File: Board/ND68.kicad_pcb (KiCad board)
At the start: 2 copper layers, 3.4 x 3 mm, 38 parts, among them J1 USB_C_Receptacle_USB2.0_14P, J2 Conn_01x03_Pin, U1 NCP1117-3.3_SOT223, U2 RP2040, Y1 Crystal_GND24

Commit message: VERY BASIC pcb layout
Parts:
- D1, D2, D3, D4: moved to B.Cu
- moved SW1 88.9 mm to (169.6, 81.3)
- moved SW3 88.9 mm to (169.6, 100.3)
- moved SW2 88.9 mm to (188.6, 81.3)
- moved SW4 88.9 mm to (188.6, 100.3)
- moved J2 77.4 mm to (142.9, 109.6), turned to 180 degrees
- moved J1 76.5 mm to (148.1, 73.6), turned to 180 degrees
- moved C2 76.3 mm to (133.3, 87.4), turned to -90 degrees
- moved C1 74.8 mm to (137.2, 87.4), turned to -90 degrees
- moved C7 72.8 mm to (153.2, 92.7), turned to 90 degrees
- moved C6 70.7 mm to (151.6, 92.7), turned to 90 degrees
- moved R2 70.0 mm to (146.1, 81.1), turned to -90 degrees
- moved C3 69.5 mm to (150.7, 92.7), turned to 90 degrees
- moved R1 68.7 mm to (150.0, 81.1), turned to -90 degrees
- moved R5 67.8 mm to (149.4, 92.7), turned to -90 degrees
- moved R6 66.3 mm to (148.4, 92.7), turned to -90 degrees
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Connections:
- R1 pad 1: Net-(J1-CC2) -> Net-(J1-CC1)
- R2 pad 1: Net-(J1-CC1) -> Net-(J1-CC2)

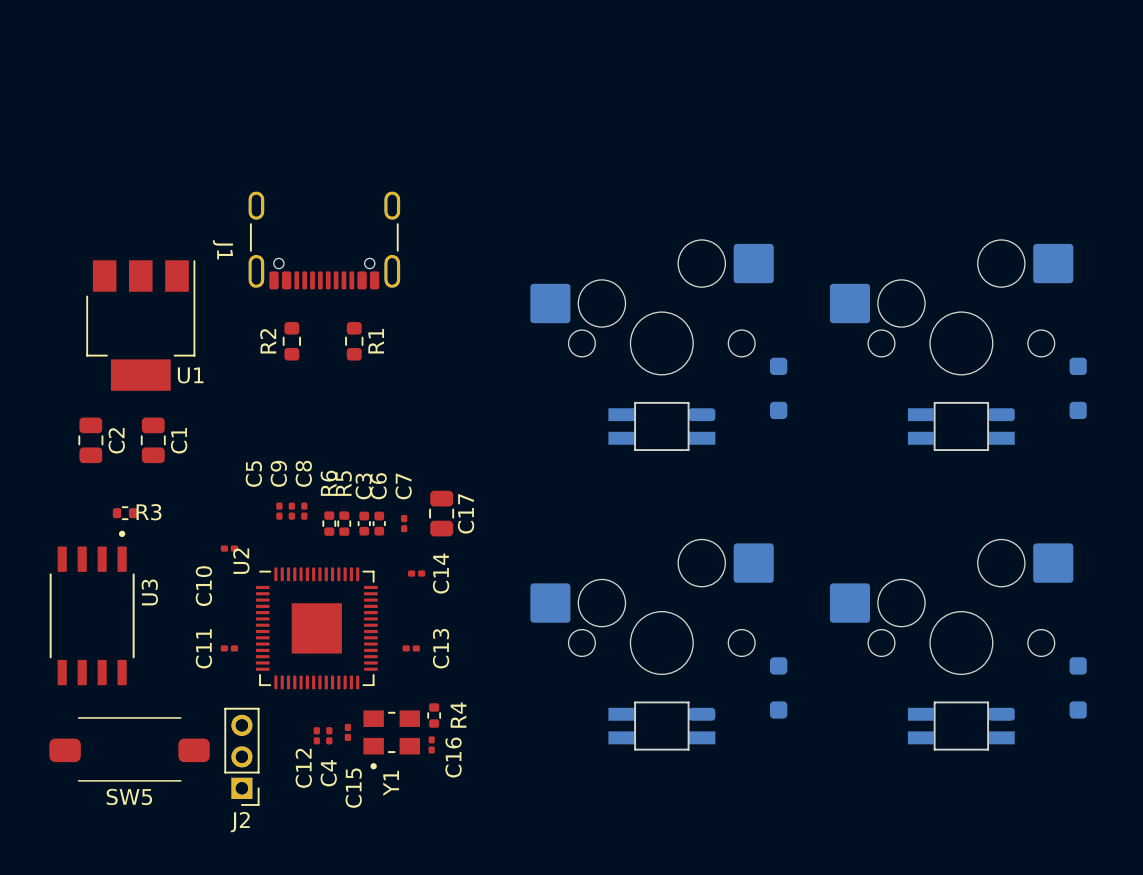
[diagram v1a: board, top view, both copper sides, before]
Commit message: Fixed pad numbers on 1u argb hotswap footprint and added a border to the pcb :)
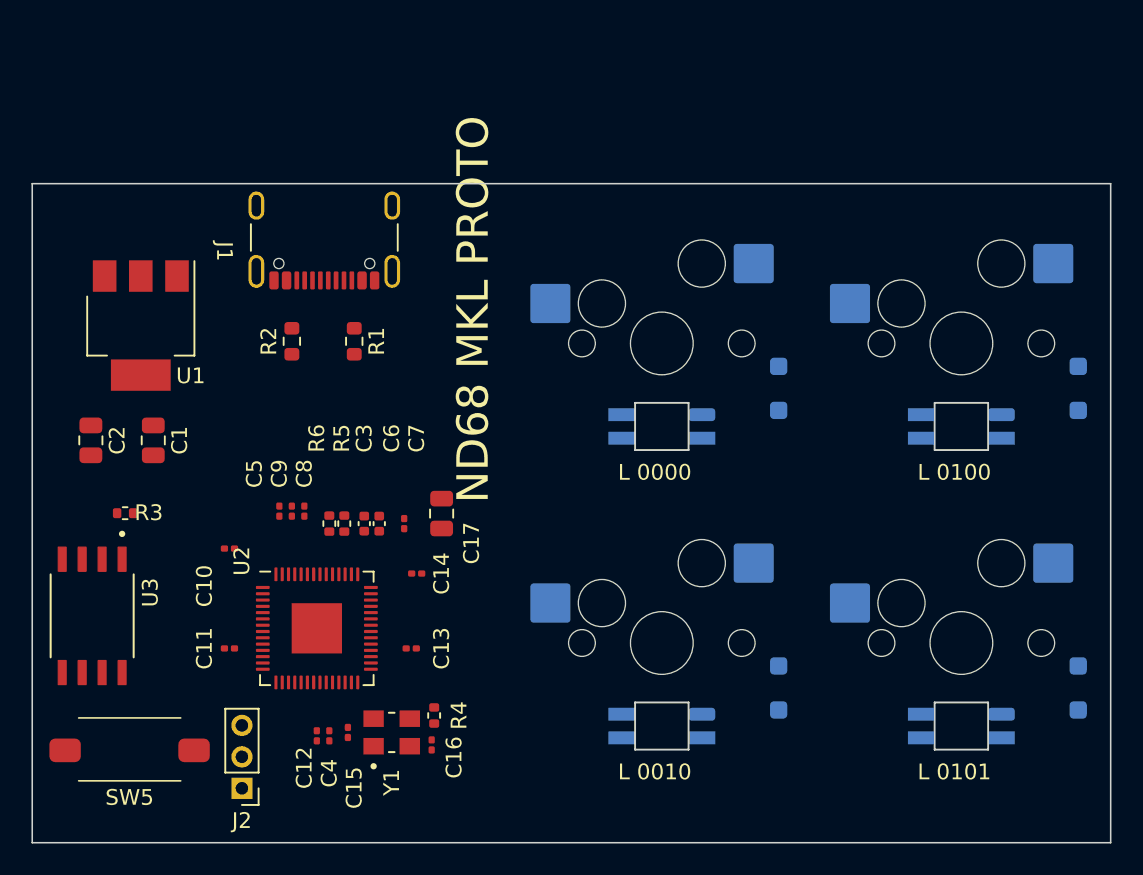
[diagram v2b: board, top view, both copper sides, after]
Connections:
- SW1 pad 1: (no net) -> VDD
- SW1 pad 2: (no net) -> Net-(SW1-DOUT)
- SW1 pad 3: (no net) -> GND
- SW1 pad 4: (no net) -> DIN
- SW2 pad 1: (no net) -> VDD
- SW2 pad 2: (no net) -> Net-(SW2-DOUT)
- SW2 pad 3: (no net) -> GND
- SW2 pad 4: (no net) -> Net-(SW1-DOUT)
- SW3 pad 1: (no net) -> VDD
- SW3 pad 2: (no net) -> Net-(SW3-DOUT)
- SW3 pad 3: (no net) -> GND
- SW3 pad 4: (no net) -> Net-(SW2-DOUT)
- SW4 pad 1: (no net) -> VDD
- SW4 pad 2: (no net) -> unconnected-(SW4-DOUT-Pad2)
- SW4 pad 3: (no net) -> GND
- SW4 pad 4: (no net) -> Net-(SW3-DOUT)
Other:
- board size 3.4 x 3 mm -> 68.6 x 41.9 mm
- board text added: "ND68 MKL PROTO"

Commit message: Route mcu
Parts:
- moved C17 19.7 mm to (141.2, 105.6), turned to -90 degrees
- moved C1 13.8 mm to (131.3, 75.0)
- moved J2 13.6 mm to (156.4, 108.0)
- moved R3 11.9 mm to (132.6, 103.6), turned to 90 degrees
- moved U3 9.19 mm to (138.9, 91.3), turned to 0 degrees
- moved C15 6.61 mm to (143.1, 107.2)
- moved C16 6.61 mm to (148.4, 108.0)
- moved R4 6.61 mm to (148.6, 106.1)
- moved Y1 6.61 mm to (145.9, 107.2)
- moved C2 4.12 mm to (135.2, 83.8)
- moved SW5 3.26 mm to (135.8, 103.9), turned to -90 degrees
- moved U1 3.15 mm to (136.5, 77.0)
- moved C12 2.93 mm to (150.5, 105.6), turned to 0 degrees
- moved C4 2.52 mm to (150.5, 104.8), turned to 0 degrees
- moved C10 2.38 mm to (142.0, 96.7)
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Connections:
- SW1 pad 5: (no net) -> Net-(D1-A)
- SW1 pad 6: (no net) -> C0
- SW2 pad 5: (no net) -> Net-(D2-A)
- SW2 pad 6: (no net) -> C1
- SW3 pad 5: (no net) -> Net-(D4-A)
- SW3 pad 6: (no net) -> C0
- SW4 pad 5: (no net) -> Net-(D3-A)
- SW4 pad 6: (no net) -> C1
- SW5 pad 1: (no net) -> GND
- SW5 pad 2: (no net) -> Net-(R3-Pad1)
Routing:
- net +3.3V: track 0.00 -> 33.3 mm
- net QSPI_SS: track 0.00 -> 27.5 mm
- net QSPI_SD1: track 0.00 -> 17.0 mm
- net D+: track 0.00 -> 14.7 mm
- net D-: track 0.00 -> 14.6 mm
- net QSPI_SD2: track 0.00 -> 12.8 mm
- net Net-(J2-Pin_1): track 0.00 -> 11.2 mm
- net +1V1: track 0.00 -> 10.6 mm
- net Net-(J2-Pin_3): track 0.00 -> 8.11 mm
- net XIN: track 0.00 -> 8.01 mm
- net QSPI_SD3: track 0.00 -> 7.57 mm
- net QSPI_SCLK: track 0.00 -> 6.55 mm
- net QSPI_SD0: track 0.00 -> 5.53 mm
- net Net-(R3-Pad1): track 0.00 -> 5.19 mm
- net GND: track 0.00 -> 3.60 mm
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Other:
- board size 68.6 x 41.9 mm -> 69.4 x 40.3 mm
- board text added: "CLK SWD"

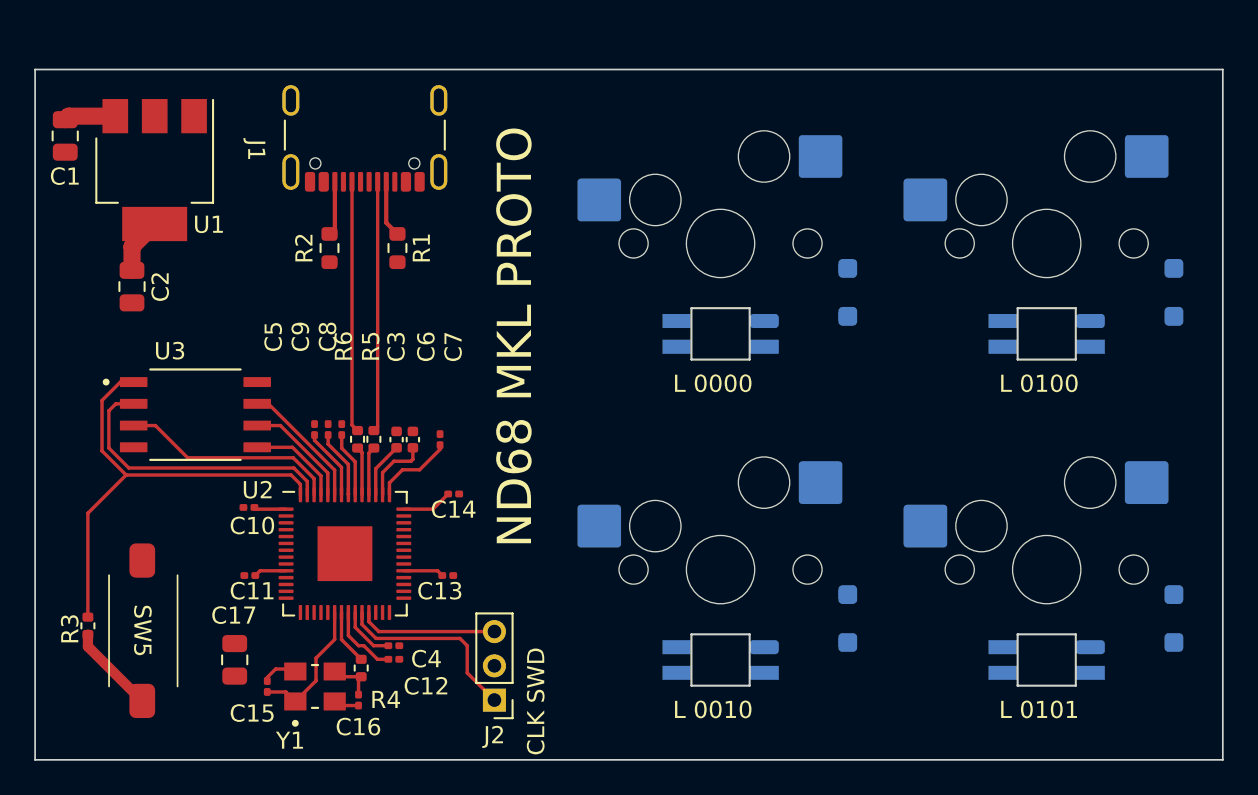
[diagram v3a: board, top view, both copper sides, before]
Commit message: Done routing all parts.
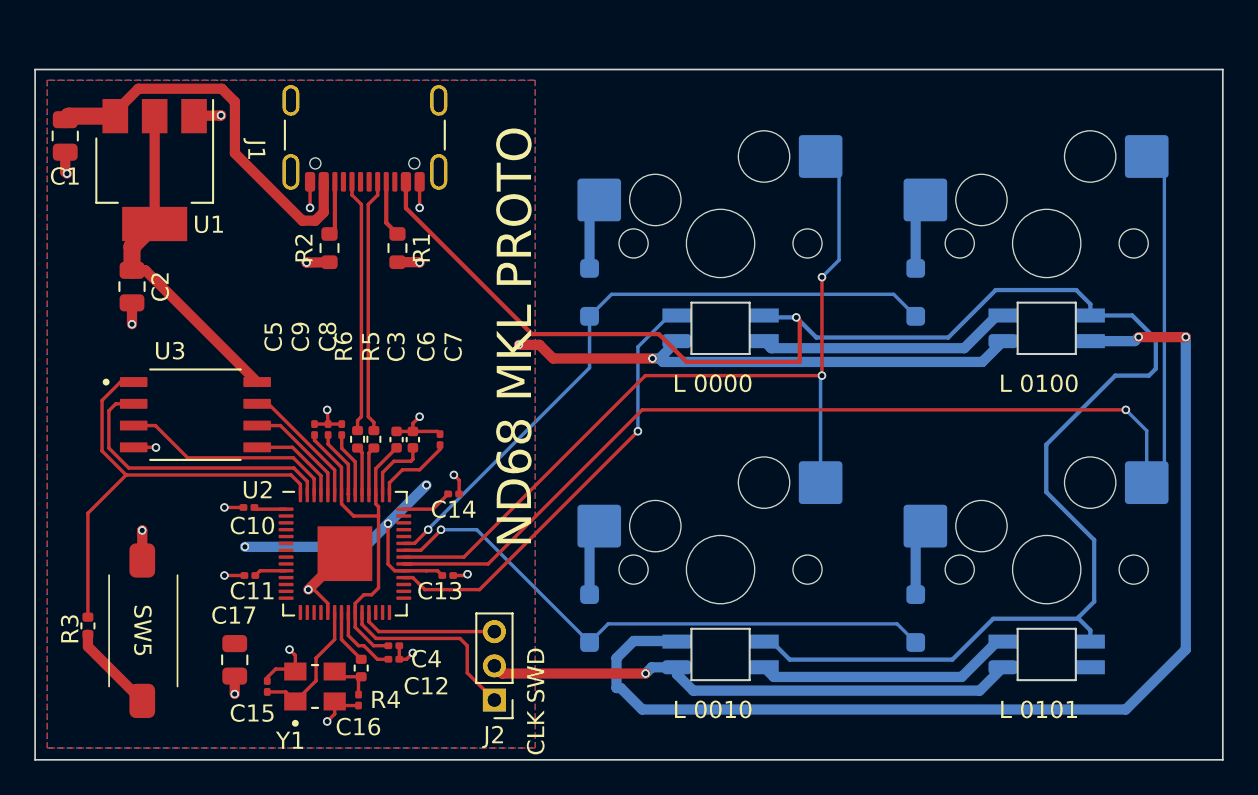
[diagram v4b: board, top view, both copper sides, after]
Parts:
- added G***: LOGO, ND68:troll, B.Cu at (143.8, 87.8)
- moved D2 15.1 mm to (181.0, 84.1)
- moved D4 15.1 mm to (181.0, 103.2)
- moved D1 15.1 mm to (161.9, 84.1)
- moved D3 15.1 mm to (161.9, 103.2)
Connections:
- SW1 pad 1: VDD -> VBUS
- SW2 pad 1: VDD -> VBUS
- SW3 pad 1: VDD -> VBUS
- SW3 pad 5: Net-(D4-A) -> Net-(D3-A)
- SW4 pad 1: VDD -> VBUS
- SW4 pad 5: Net-(D3-A) -> Net-(D4-A)
- U2 pad 32: unconnected-(U2-GPIO21-Pad32) -> DIN
- U2 pad 34: unconnected-(U2-GPIO22-Pad34) -> C1
- U2 pad 35: unconnected-(U2-GPIO23-Pad35) -> C0
- U2 pad 36: unconnected-(U2-GPIO24-Pad36) -> R1
- U2 pad 37: unconnected-(U2-GPIO25-Pad37) -> R0
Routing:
- net VBUS: track 3.01 -> 123.5 mm, vias 0 -> 1
- net GND: track 3.60 -> 99.3 mm, vias 0 -> 23
- net C1: track 0.00 -> 71.0 mm, vias 0 -> 1
- net Net-(SW2-DOUT): track 0.00 -> 64.8 mm, vias 0 -> 2
- net C0: track 0.00 -> 50.3 mm, vias 0 -> 2
- net R0: track 0.00 -> 38.2 mm, vias 0 -> 1
- net R1: track 0.00 -> 34.0 mm, vias 0 -> 1
- net +3.3V: track 33.3 -> 65.3 mm, vias 0 -> 3
- net DIN: track 0.00 -> 25.8 mm, vias 0 -> 1
- net Net-(SW3-DOUT): track 0.00 -> 15.0 mm
- net Net-(SW1-DOUT): track 0.00 -> 14.9 mm
- net +1V1: track 10.6 -> 21.4 mm
- net Net-(D2-A): track 0.00 -> 4.23 mm
- net Net-(D4-A): track 0.00 -> 4.23 mm
- net Net-(D1-A): track 0.00 -> 4.23 mm
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- added copper zone on F.Cu, net +3.3V
- added copper zone on B.Cu, net GND

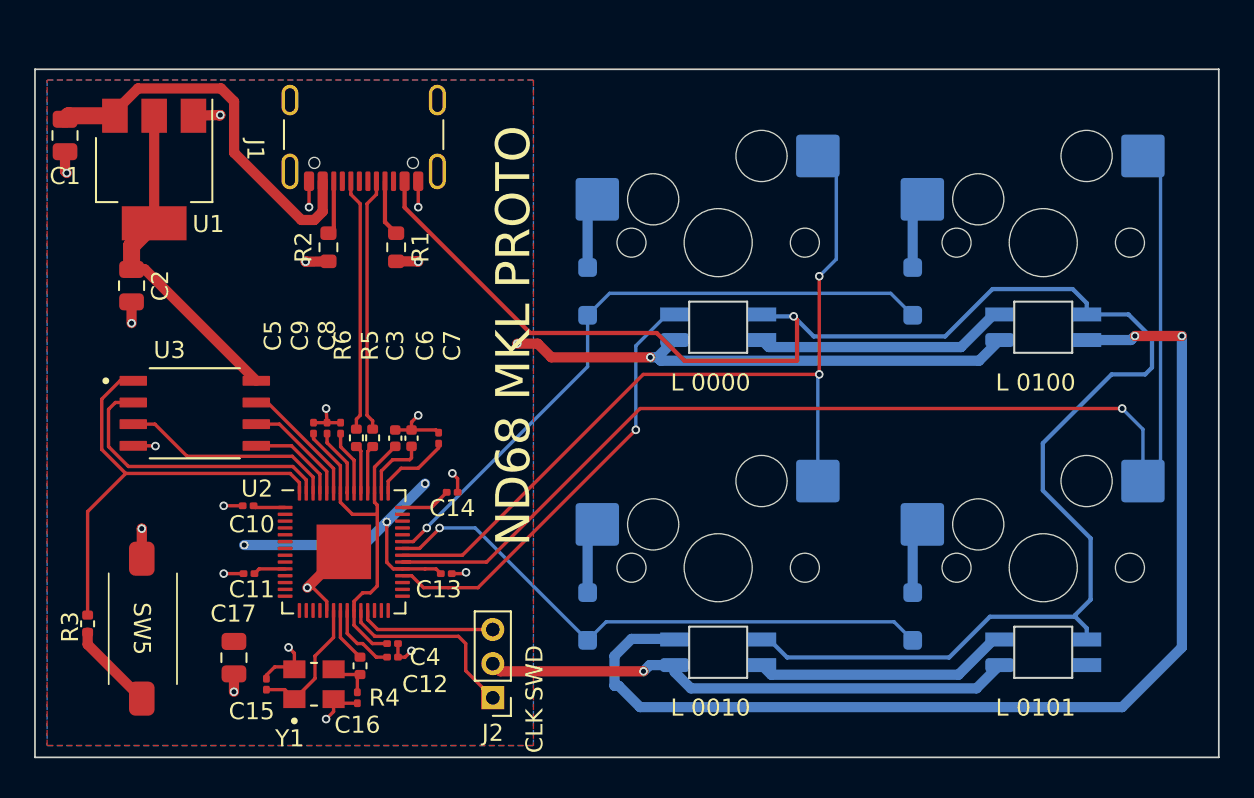
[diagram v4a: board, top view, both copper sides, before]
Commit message: Fixed coupling issues and cleaned up board
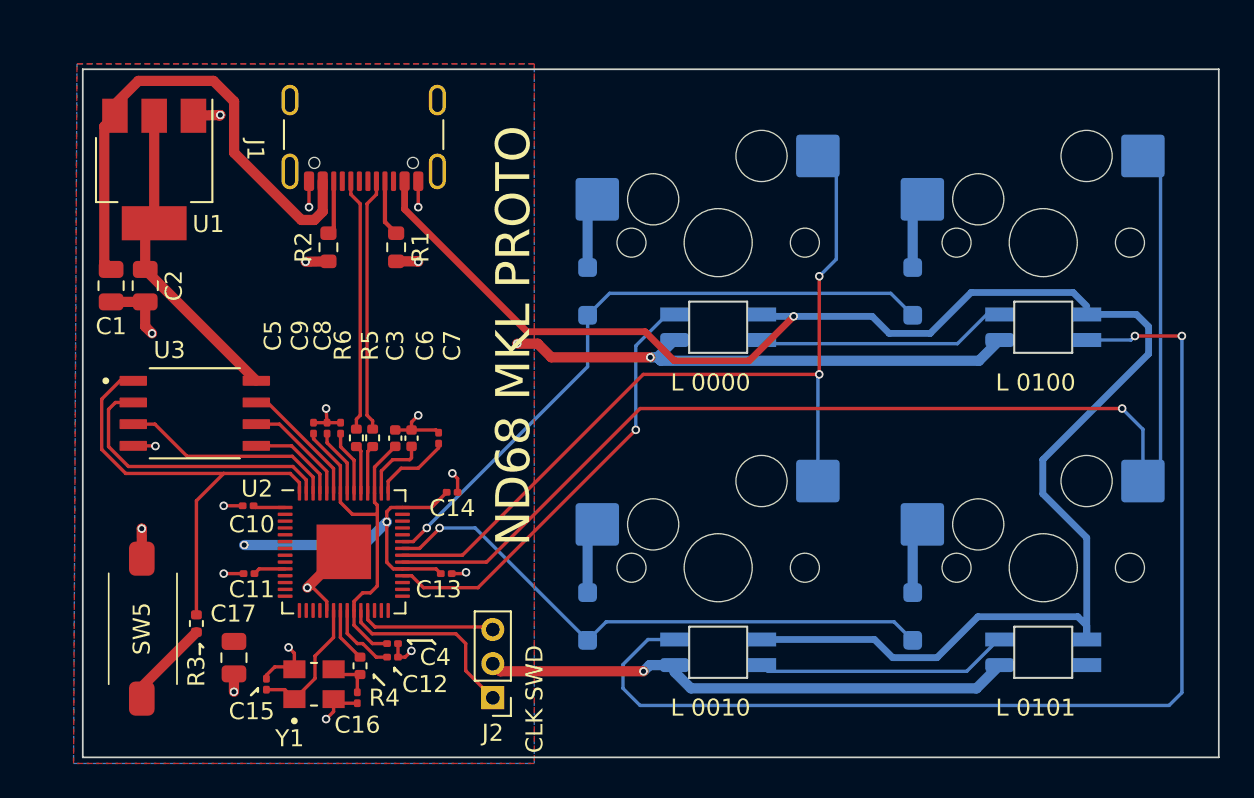
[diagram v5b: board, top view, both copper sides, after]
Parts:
- moved C1 9.20 mm to (134.0, 83.8)
- moved R3 6.38 mm to (139.0, 103.6)
- moved C2 0.80 mm to (136.0, 83.8)
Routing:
- net +3.3V: track 65.3 -> 61.6 mm, vias 3 -> 2
- net VBUS: track 123.5 -> 127.1 mm
- net C1: track 71.0 -> 67.6 mm
- net C0: track 50.3 -> 47.2 mm
- net GND: track 99.3 -> 100.1 mm, vias 23 -> 22
- net Net-(D4-A): track 4.23 -> 3.43 mm
- net Net-(D2-A): track 4.23 -> 3.43 mm
- net Net-(D3-A): track 4.23 -> 3.43 mm
- net Net-(D1-A): track 4.23 -> 3.43 mm
- net Net-(R3-Pad1): track 5.19 -> 4.53 mm
- net Net-(C16-Pad2): track 2.78 -> 2.13 mm
- net QSPI_SD3: track 7.57 -> 6.92 mm
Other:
- board size 69.4 x 40.3 mm -> 66.6 x 40.3 mm
